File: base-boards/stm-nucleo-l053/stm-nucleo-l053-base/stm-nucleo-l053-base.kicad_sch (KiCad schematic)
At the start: 2 parts, among them U1 NUCLEO-L053R8

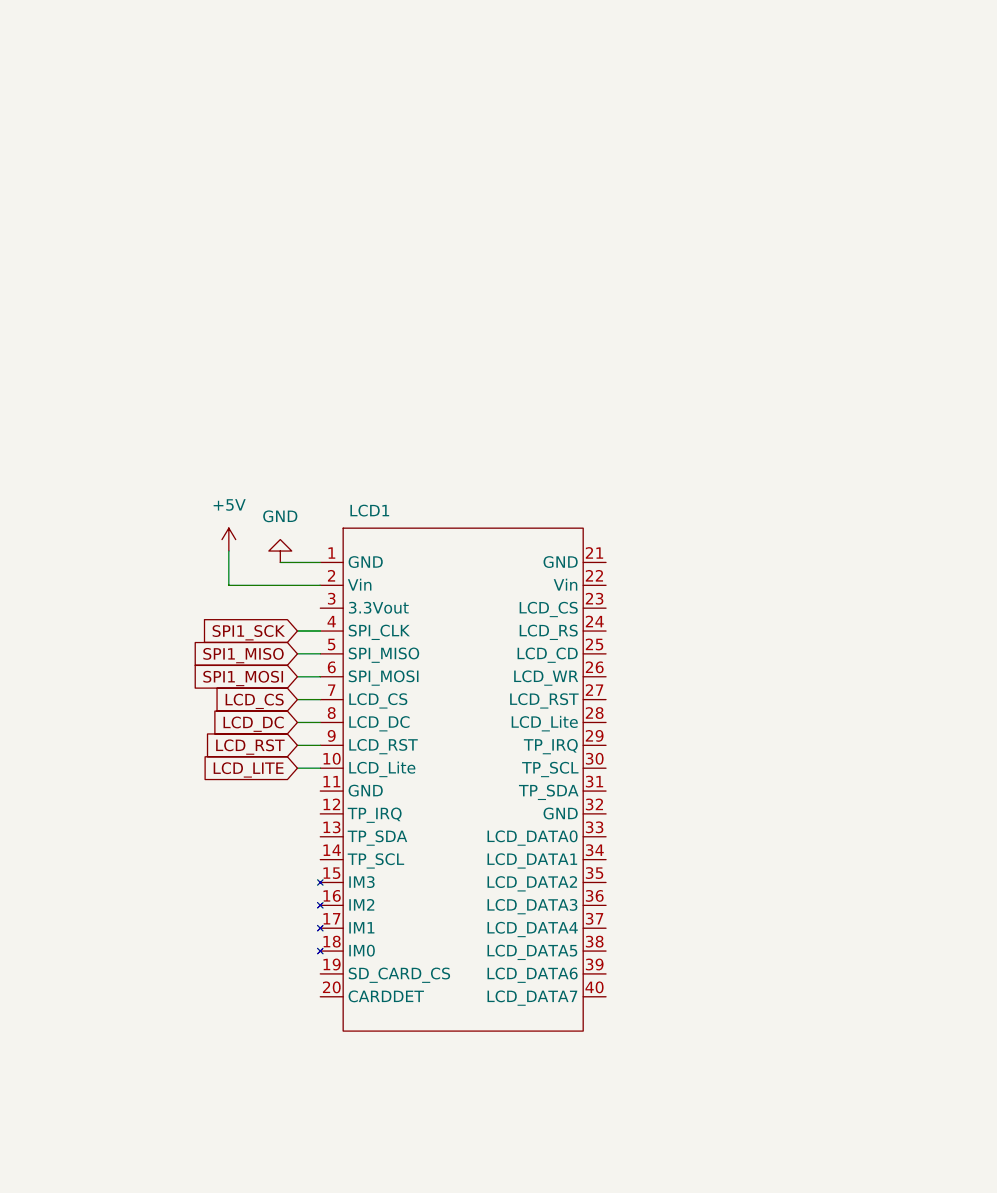
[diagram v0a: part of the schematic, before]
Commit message: Added Arduino Nano breakout
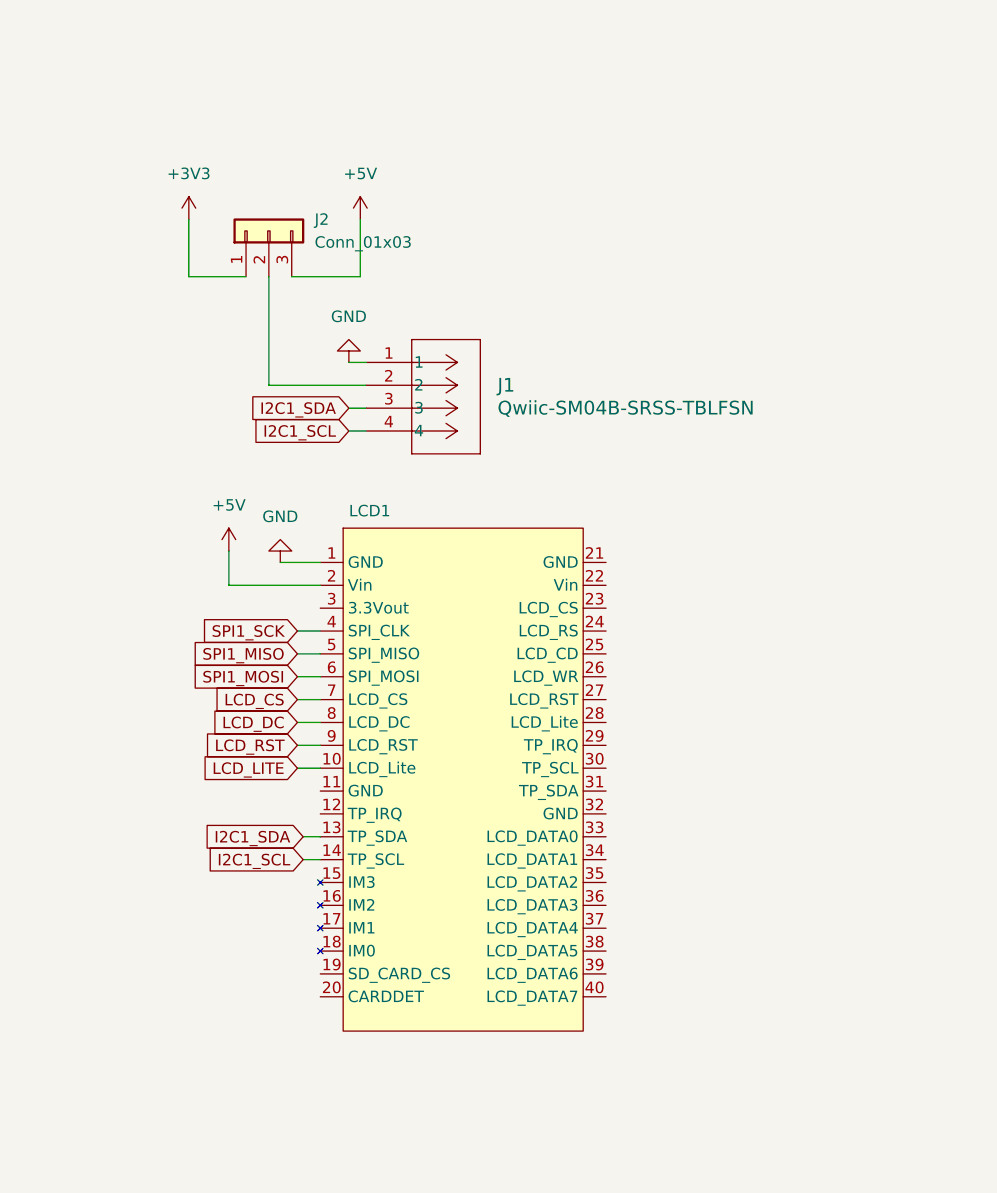
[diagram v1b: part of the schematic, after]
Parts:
- added J1: Qwiic-SM04B-SRSS-TBLFSN, KPM-Connectors:CONN_Qwiic_SM04B_JST, symbol KPM-Connectors:Qwiic-SM04B-SRSS-TBLFSN
- added J2: Conn_01x03, Connector_PinHeader_2.54mm:PinHeader_1x03_P2.54mm_Vertical, symbol Connector_Generic:Conn_01x03
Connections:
- net +3V3: now also J2.1 (Pin_1)
- net +5V: now also J2.3 (Pin_3)
- net GND: now also J1.1
- net I2C1_SCL: now also LCD1.14 (TP_SCL), J1.4
- net I2C1_SDA: now also LCD1.13 (TP_SDA), J1.3
- new net: J1.2, J2.2 (Pin_2)
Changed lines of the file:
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@@
+    (stroke (width 0) (type default))
+  )
+  (wire (pts (xy 144.78 60.325) (xy 155.575 60.325))
     (stroke (width 0) (type default))
   )
@@
     (stroke (width 0) (type default))
   )
+  (wire (pts (xy 135.89 41.91) (xy 135.89 48.26))
+    (stroke (width 0) (type default))
+  )
+  (wire (pts (xy 153.67 57.785) (xy 155.575 57.785))
+    (stroke (width 0) (type default))
+  )
   (wire (pts (xy 73.66 158.115) (xy 80.01 158.115))
     (stroke (width 0) (type default))
@@
     (stroke (width 0) (type default))
   )
+  (wire (pts (xy 148.59 113.03) (xy 150.495 113.03))
+    (stroke (width 0) (type default))
+  )
   (wire (pts (xy 146.05 80.01) (xy 150.495 80.01))
     (stroke (width 0) (type default))
@@
     (stroke (width 0) (type default))
   )
+  (wire (pts (xy 154.94 41.91) (xy 154.94 48.26))
+    (stroke (width 0) (type default))
+  )
   (wire (pts (xy 147.955 90.17) (xy 150.495 90.17))
     (stroke (width 0) (type default))
@@
     (stroke (width 0) (type default))
   )
+  (wire (pts (xy 142.24 48.26) (xy 135.89 48.26))
+    (stroke (width 0) (type default))
+  )
   (wire (pts (xy 40.005 88.9) (xy 41.91 88.9))
     (stroke (width 0) (type default))
@@
     (stroke (width 0) (type default))
   )
+  (wire (pts (xy 144.78 48.26) (xy 144.78 60.325))
+    (stroke (width 0) (type default))
+  )
   (wire (pts (xy 40.005 91.44) (xy 41.91 91.44))
     (stroke (width 0) (type default))
   )
+  (wire (pts (xy 147.32 48.26) (xy 154.94 48.26))
+    (stroke (width 0) (type default))
+  )
   (wire (pts (xy 94.615 46.99) (xy 94.615 48.26))
     (stroke (width 0) (type default))
@@
     (stroke (width 0) (type default))
   )
+  (wire (pts (xy 153.67 65.405) (xy 155.575 65.405))
+    (stroke (width 0) (type default))
+  )
   (wire (pts (xy 39.37 104.14) (xy 41.91 104.14))
     (stroke (width 0) (type default))
@@
     (stroke (width 0) (type default))
   )
+  (wire (pts (xy 148.59 110.49) (xy 150.495 110.49))
+    (stroke (width 0) (type default))
+  )
   (wire (pts (xy 73.66 155.575) (xy 80.01 155.575))
     (stroke (width 0) (type default))
@@
   )
   (wire (pts (xy 41.91 96.52) (xy 24.765 96.52))
+    (stroke (width 0) (type default))
+  )
+  (wire (pts (xy 153.67 62.865) (xy 155.575 62.865))
     (stroke (width 0) (type default))
   )
@@
     )
   )
+  (global_label "I2C1_SCL" (shape input) (at 148.59 113.03 180) (fields_autoplaced)
+    (effects (font (size 1.27 1.27)) (justify right))
+    (property "Intersheetrefs" "${INTERSHEET_REFS}" (at 136.8358 113.03 0)
+      (effects (font (size 1.27 1.27)) (justify right) hide)
+    )
+  )
   (global_label "SPI1_SCK" (shape input) (at 147.955 87.63 180) (fields_autoplaced)
     (effects (font (size 1.27 1.27)) (justify right))
@@
     )
   )
+  (global_label "I2C1_SDA" (shape input) (at 153.67 62.865 180) (fields_autoplaced)
+    (effects (font (size 1.27 1.27)) (justify right))
+    (property "Intersheetrefs" "${INTERSHEET_REFS}" (at 141.8553 62.865 0)
+      (effects (font (size 1.27 1.27)) (justify right) hide)
+    )
+  )
   (global_label "LCD_LITE" (shape input) (at 147.955 102.87 180) (fields_autoplaced)
     (effects (font (size 1.27 1.27)) (justify right))
@@
     )
   )
+  (global_label "I2C1_SDA" (shape input) (at 148.59 110.49 180) (fields_autoplaced)
+    (effects (font (size 1.27 1.27)) (justify right))
+    (property "Intersheetrefs" "${INTERSHEET_REFS}" (at 136.7753 110.49 0)
+      (effects (font (size 1.27 1.27)) (justify right) hide)
+    )
+  )
   (global_label "I2C1_SDA" (shape input) (at 40.005 91.44 180) (fields_autoplaced)
     (effects (font (size 1.27 1.27)) (justify right))
@@
     )
   )
+  (global_label "I2C1_SCL" (shape input) (at 153.67 65.405 180) (fields_autoplaced)
+    (effects (font (size 1.27 1.27)) (justify right))
+    (property "Intersheetrefs" "${INTERSHEET_REFS}" (at 141.9158 65.405 0)
+      (effects (font (size 1.27 1.27)) (justify right) hide)
+    )
+  )
   (global_label "I2C1_SCL" (shape input) (at 40.005 88.9 180) (fields_autoplaced)
     (effects (font (size 1.27 1.27)) (justify right))
@@
         (path "/e40fcfd6-4070-4bae-bfa8-988e9cebe59d"
           (reference "#PWR01") (unit 1)
+        )
+      )
+    )
+  )
+  (symbol (lib_id "power:GND") (at 153.67 57.785 180) (unit 1)
+    (in_bom yes) (on_board yes) (dnp no) (fields_autoplaced)
+    (property "Reference" "#PWR019" (at 153.67 51.435 0)
+      (effects (font (size 1.27 1.27)) hide)
+    )
+    (property "Value" "GND" (at 153.67 52.705 0)
+      (effects (font (size 1.27 1.27)))
+    )
+    (property "Footprint" "" (at 153.67 57.785 0)
+      (effects (font (size 1.27 1.27)) hide)
+    )
+    (property "Datasheet" "" (at 153.67 57.785 0)
+      (effects (font (size 1.27 1.27)) hide)
+    )
+    (pin "1")
+    (instances
+      (project "stm-nucleo-l053-base"
+        (path "/e40fcfd6-4070-4bae-bfa8-988e9cebe59d"
+          (reference "#PWR019") (unit 1)
         )
       )
@@
     )
   )
+  (symbol (lib_id "power:+5V") (at 154.94 41.91 0) (unit 1)
+    (in_bom yes) (on_board yes) (dnp no) (fields_autoplaced)
+    (property "Reference" "#PWR020" (at 154.94 45.72 0)
+      (effects (font (size 1.27 1.27)) hide)
+    )
+    (property "Value" "+5V" (at 154.94 36.83 0)
+      (effects (font (size 1.27 1.27)))
+    )
+    (property "Footprint" "" (at 154.94 41.91 0)
+      (effects (font (size 1.27 1.27)) hide)
+    )
+    (property "Datasheet" "" (at 154.94 41.91 0)
+      (effects (font (size 1.27 1.27)) hide)
+    )
+    (pin "1")
+    (instances
+      (project "stm-nucleo-l053-base"
+        (path "/e40fcfd6-4070-4bae-bfa8-988e9cebe59d"
+          (reference "#PWR020") (unit 1)
+        )
+      )
+    )
+  )
   (symbol (lib_id "power:GND") (at 94.615 48.26 0) (unit 1)
     (in_bom yes) (on_board yes) (dnp no) (fields_autoplaced)
@@
         (path "/e40fcfd6-4070-4bae-bfa8-988e9cebe59d"
           (reference "#PWR05") (unit 1)
+        )
+      )
+    )
+  )
+  (symbol (lib_id "KPM-Connectors:Qwiic-SM04B-SRSS-TBLFSN") (at 155.575 57.785 0) (unit 1)
+    (in_bom yes) (on_board yes) (dnp no) (fields_autoplaced)
+    (property "Reference" "J1" (at 170.18 60.325 0)
+      (effects (font (size 1.524 1.524)) (justify left))
+    )
+    (property "Value" "Qwiic-SM04B-SRSS-TBLFSN" (at 170.18 62.865 0)
+      (effects (font (size 1.524 1.524)) (justify left))
+    )
+    (property "Footprint" "KPM-Connectors:CONN_Qwiic_SM04B_JST" (at 155.575 57.785 0)
+      (effects (font (size 1.27 1.27) italic) hide)
+    )
+    (property "Datasheet" "SM04B-SRSS-TBLFSN" (at 155.575 57.785 0)
+      (effects (font (size 1.27 1.27) italic) hide)
+    )
+    (pin "1")
+    (pin "2")
+    (pin "3")
+    (pin "4")
+    (instances
+      (project "stm-nucleo-l053-base"
+        (path "/e40fcfd6-4070-4bae-bfa8-988e9cebe59d"
+          (reference "J1") (unit 1)
         )
       )
@@
     )
   )
+  (symbol (lib_id "power:+3V3") (at 135.89 41.91 0) (unit 1)
+    (in_bom yes) (on_board yes) (dnp no) (fields_autoplaced)
+    (property "Reference" "#PWR021" (at 135.89 45.72 0)
+      (effects (font (size 1.27 1.27)) hide)
+    )
+    (property "Value" "+3V3" (at 135.89 36.83 0)
+      (effects (font (size 1.27 1.27)))
+    )
+    (property "Footprint" "" (at 135.89 41.91 0)
+      (effects (font (size 1.27 1.27)) hide)
+    )
+    (property "Datasheet" "" (at 135.89 41.91 0)
+      (effects (font (size 1.27 1.27)) hide)
+    )
+    (pin "1")
+    (instances
+      (project "stm-nucleo-l053-base"
+        (path "/e40fcfd6-4070-4bae-bfa8-988e9cebe59d"
+          (reference "#PWR021") (unit 1)
+        )
+      )
+    )
+  )
   (symbol (lib_id "power:GND") (at 146.05 80.01 180) (unit 1)
     (in_bom yes) (on_board yes) (dnp no) (fields_autoplaced)
@@
         )
       )
+    )
+  )
+  (symbol (lib_id "Connector_Generic:Conn_01x03") (at 144.78 43.18 90) (unit 1)
+    (in_bom yes) (on_board yes) (dnp no) (fields_autoplaced)
+    (property "Reference" "J2" (at 149.86 41.91 90)
+      (effects (font (size 1.27 1.27)) (justify right))
+    )
+    (property "Value" "Conn_01x03" (at 149.86 44.45 90)
+      (effects (font (size 1.27 1.27)) (justify right))
+    )
+    (property "Footprint" "Connector_PinHeader_2.54mm:PinHeader_1x03_P2.54mm_Vertical" (at 144.78 43.18 0)
+      (effects (font (size 1.27 1.27)) hide)
+    )
+    (property "Datasheet" "~" (at 144.78 43.18 0)
+      (effects (font (size 1.27 1.27)) hide)
+    )
+    (property "Populate" "" (at 144.78 43.18 0)
+      (effects (font (size 1.27 1.27)))
+    )
+    (pin "1")
+    (pin "2")
+    (pin "3")
+    (instances
+      (project "stm-nucleo-l053-base"
+        (path "/e40fcfd6-4070-4bae-bfa8-988e9cebe59d"
+          (reference "J2") (unit 1)
+        )
+      )
